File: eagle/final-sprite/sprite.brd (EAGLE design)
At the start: 35 x 44.6 mm, 60 parts, among them J1 M20-7910442R, U1 CC430F513X, U2 LSM9DS1, U4 DRV8837, U5 ADP5092, U6 DRV8837, U7 DRV8837, X1 SPRITEPIN_SPRITE_PIN, X2 SPRITEPIN_SPRITE_PIN

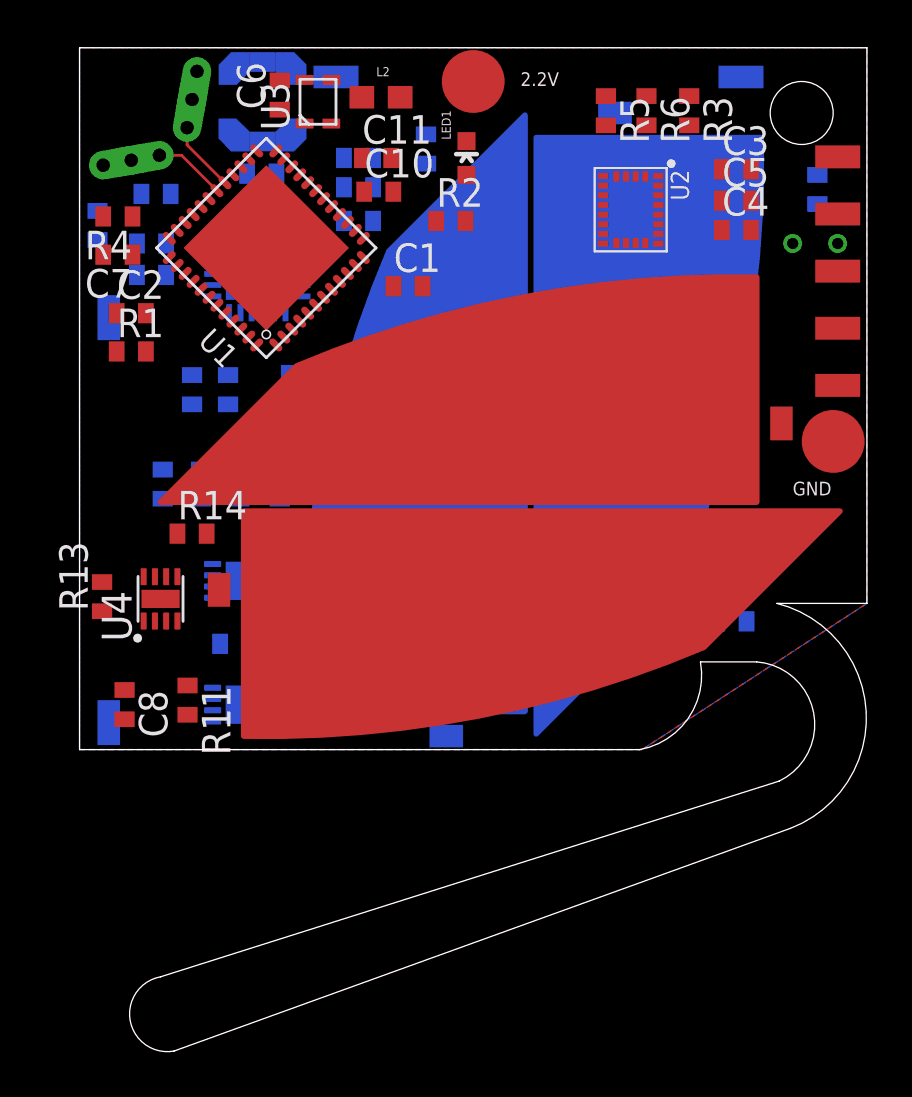
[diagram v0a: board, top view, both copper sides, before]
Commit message: successful autoroute 2 blind capability 69 vias
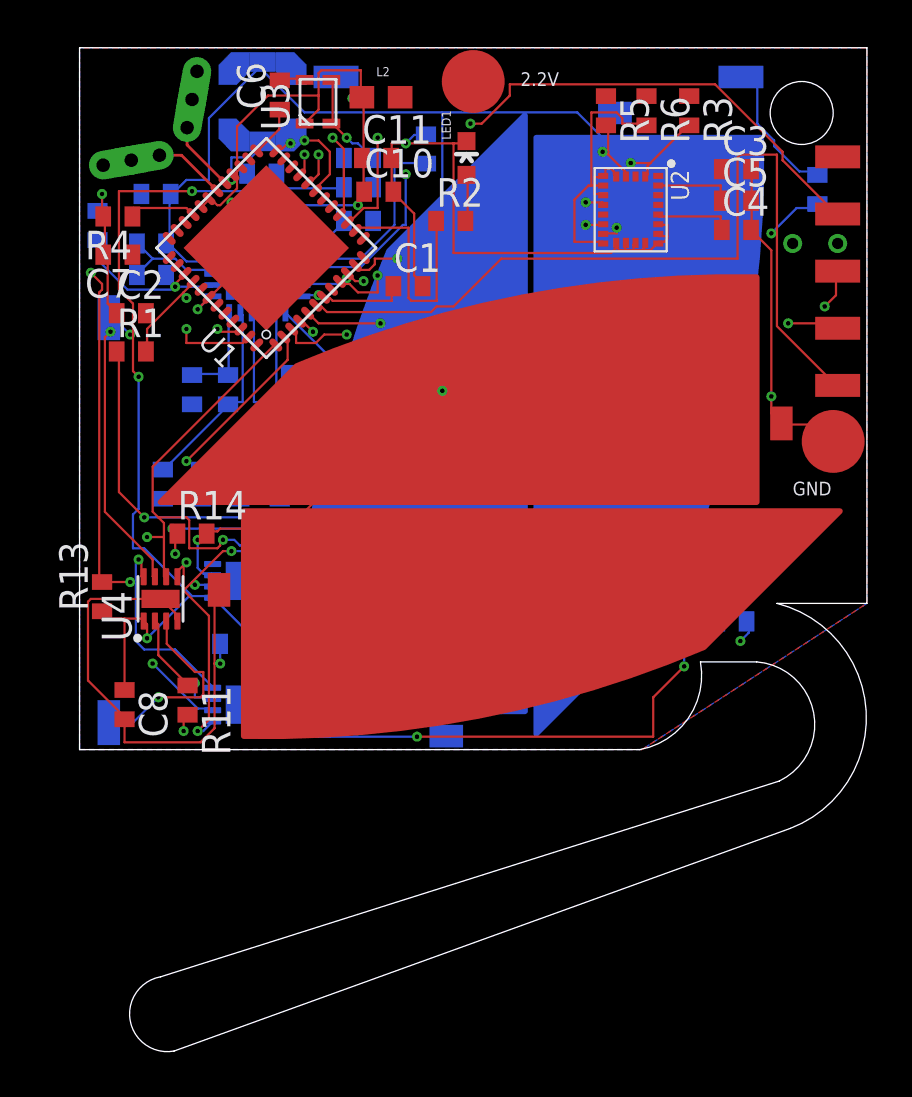
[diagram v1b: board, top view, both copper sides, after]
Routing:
- net VCCINT: track 0.00 -> 88.0 mm, vias 0 -> 1
- net GND: track 0.16 -> 86.0 mm, vias 0 -> 6
- net VCCIO: track 0.00 -> 43.4 mm, vias 0 -> 3
- net RST: track 0.00 -> 40.7 mm, vias 0 -> 2
- net UART_RX: track 0.00 -> 37.6 mm
- net N$26: track 0.00 -> 35.5 mm, vias 0 -> 2
- net VSYS: track 0.00 -> 34.3 mm, vias 0 -> 4
- net TST: track 0.00 -> 34.0 mm, vias 0 -> 2
- net PWM1: track 0.00 -> 32.3 mm, vias 0 -> 3
- net EN_2: track 0.00 -> 31.7 mm, vias 0 -> 2
- net EN_3: track 0.00 -> 28.6 mm, vias 0 -> 2
- net EN_1: track 0.00 -> 28.3 mm, vias 0 -> 2
- net VCC: track 0.00 -> 27.4 mm, vias 0 -> 2
- net VBAT: track 0.00 -> 26.5 mm, vias 0 -> 1
- net N$27: track 0.00 -> 26.5 mm, vias 0 -> 2
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
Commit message: did most of the long traces
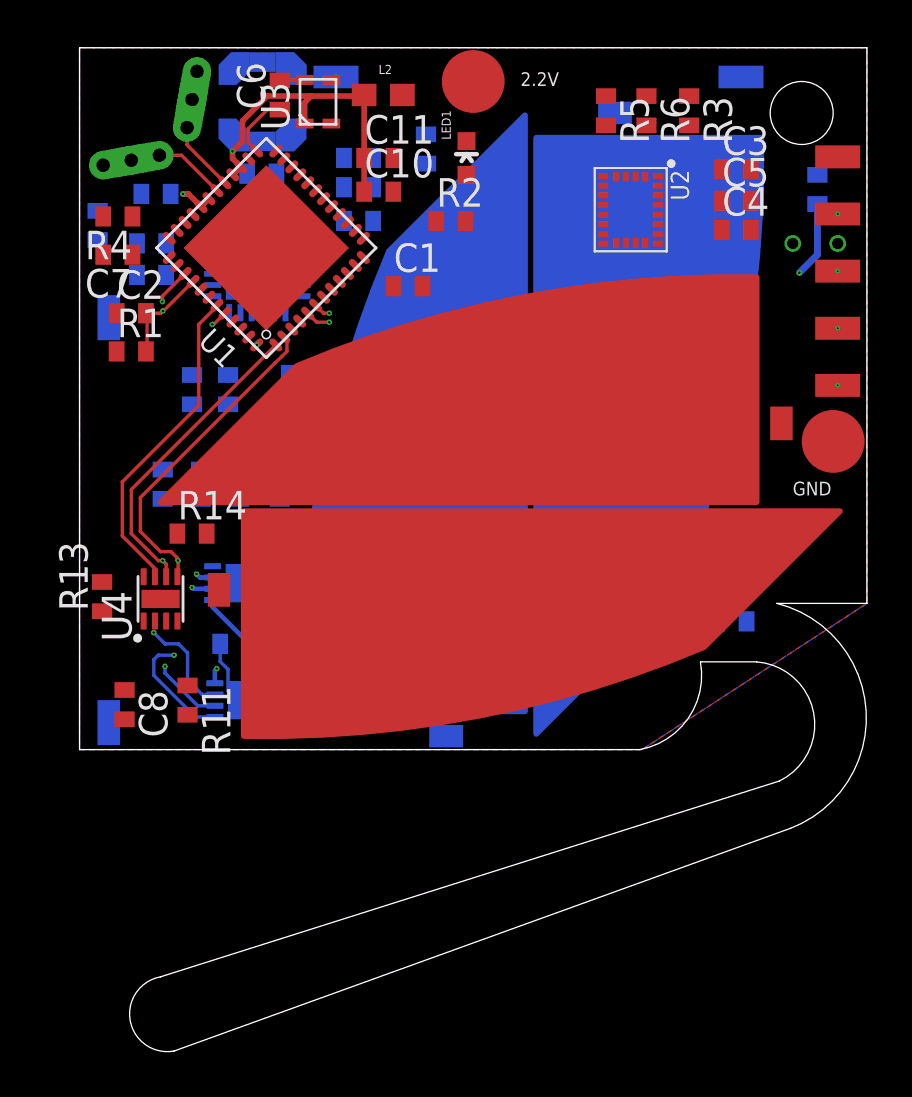
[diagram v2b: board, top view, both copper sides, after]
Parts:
- moved U7 5.40 mm to (6.90, 11.2), turned to 180 degrees
- moved U6 5.30 mm to (7.00, 6.00), turned to 0 degrees
- moved L2 0.14 mm to (13.5, 32.9)
- moved C11 0.10 mm to (13.3, 30.1)
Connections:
- removed net VSYS: C14.1, C15.1, R13.2, R14.1, U5.16
- net EN_1: now also U1.43; no longer U1.19
- net EN_2: now also U1.44; no longer U1.20
- net EN_3: now also U1.48; no longer U1.21
- net VCC: now also C14.1, C15.1, R13.2, R14.1, U5.16
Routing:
- net VCCINT: track 88.0 -> 0.00 mm, vias 1 -> 0
- net GND: track 86.0 -> 4.46 mm, vias 6 -> 0
- net VCCIO: track 43.4 -> 4.56 mm, vias 3 -> 0
- net VSYS: track 34.3 -> 0.00 mm, vias 4 -> 0
- net VCC: track 27.4 -> 4.49 mm
- net UART_TX: track 23.9 -> 45.9 mm
- net N$4: track 21.1 -> 0.00 mm, vias 2 -> 0
- net SCL: track 20.3 -> 0.00 mm, vias 2 -> 0
- net N$28: track 25.1 -> 6.83 mm, vias 2 -> 1
- net INT2: track 17.6 -> 0.00 mm, vias 2 -> 0
- net SDA: track 17.1 -> 0.00 mm, vias 2 -> 0
- net REF: track 16.6 -> 0.00 mm
- net N$13: track 23.7 -> 7.14 mm, vias 2 -> 1
- net INT1: track 16.5 -> 0.00 mm, vias 2 -> 0
- net N$27: track 26.5 -> 42.3 mm
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- added copper zone on layer 2, net GND

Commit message: more stuff done
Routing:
- net VCCINT: track 0.00 -> 31.6 mm, vias 0 -> 2
- added copper zone on layer 1, net VCCINT
- added copper zone on layer 16, net VCCINT

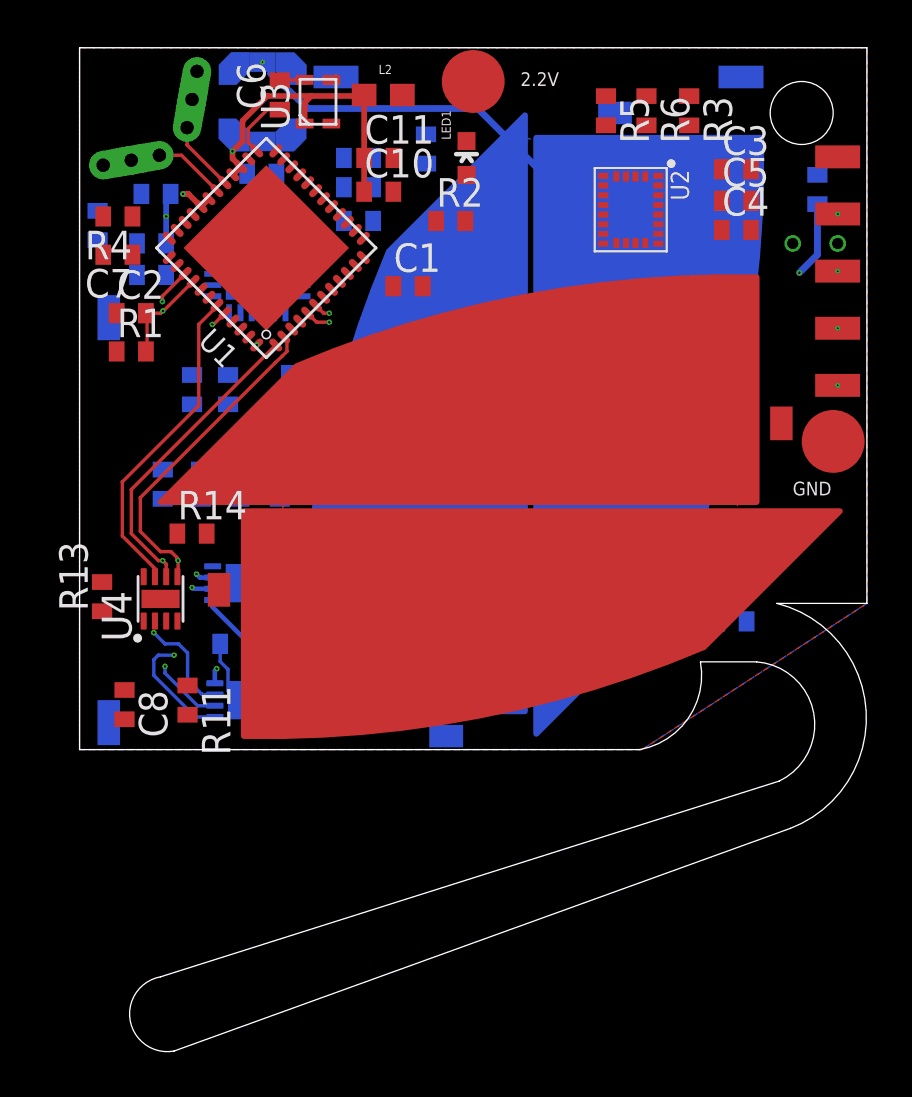
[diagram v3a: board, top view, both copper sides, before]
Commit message: routed some more routes
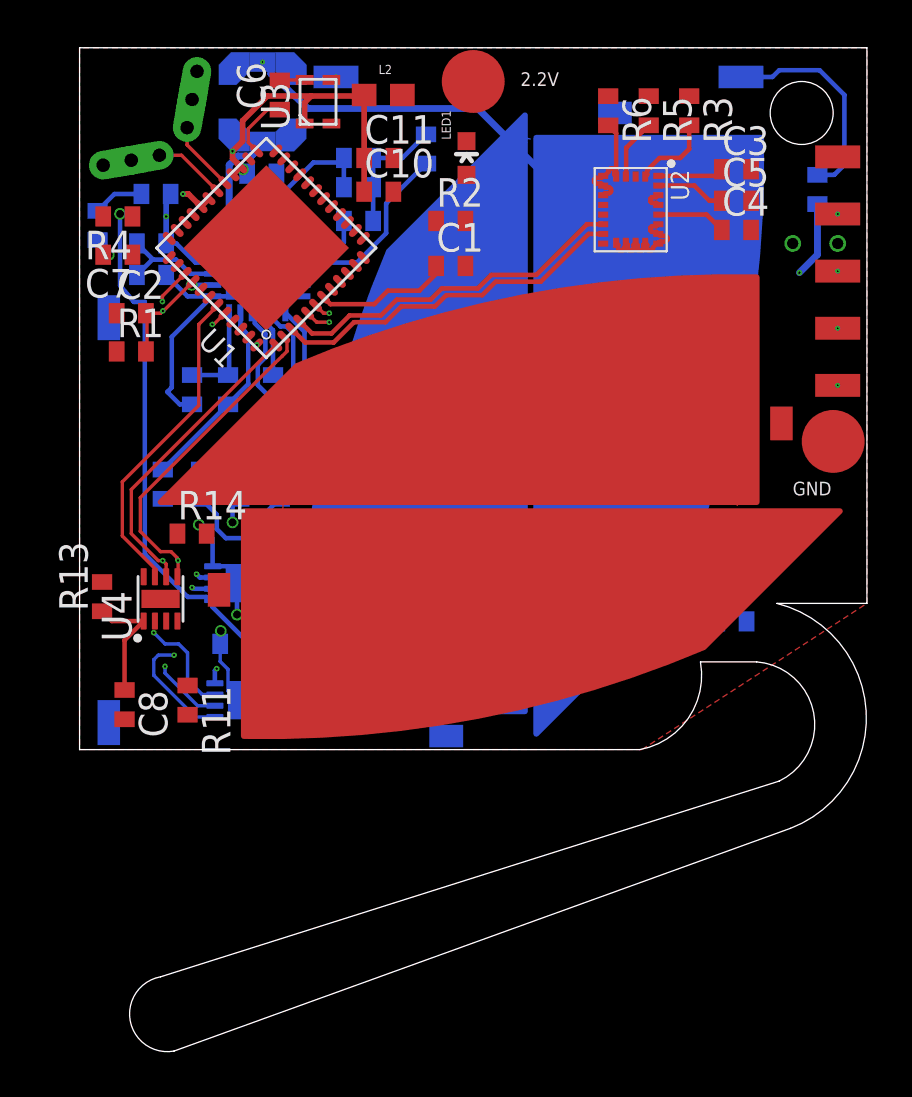
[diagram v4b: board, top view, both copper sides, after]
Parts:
- moved C1 2.10 mm to (16.5, 25.3)
- moved R5 1.90 mm to (25.3, 32.2)
- moved R6 1.70 mm to (23.5, 32.2)
- moved R21 0.81 mm to (8.60, 19.8)
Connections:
- net INT1: now also U1.4; no longer U1.3
- net INT2: now also U1.3; no longer U1.4
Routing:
- net GND: track 4.46 -> 47.1 mm, vias 0 -> 4
- net VCCIO: track 4.56 -> 39.1 mm, vias 0 -> 2
- net REF: track 0.00 -> 16.8 mm
- net INT2: track 0.00 -> 16.1 mm
- net INT1: track 0.00 -> 15.7 mm
- net VCC: track 4.49 -> 14.7 mm
- net TERM: track 0.00 -> 9.99 mm
- net N$9: track 0.00 -> 9.67 mm
- net SETSD: track 0.00 -> 9.52 mm
- net SETPG: track 0.00 -> 8.66 mm
- net N$20: track 0.00 -> 8.12 mm
- net VCORE: track 0.00 -> 6.04 mm
- net N$21: track 0.00 -> 6.04 mm, vias 0 -> 2
- net N$7: track 0.00 -> 5.45 mm
- net N$18: track 0.00 -> 4.93 mm
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- removed copper zone on layer 16, net GND

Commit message: routed all traces, need to do GND and VCC
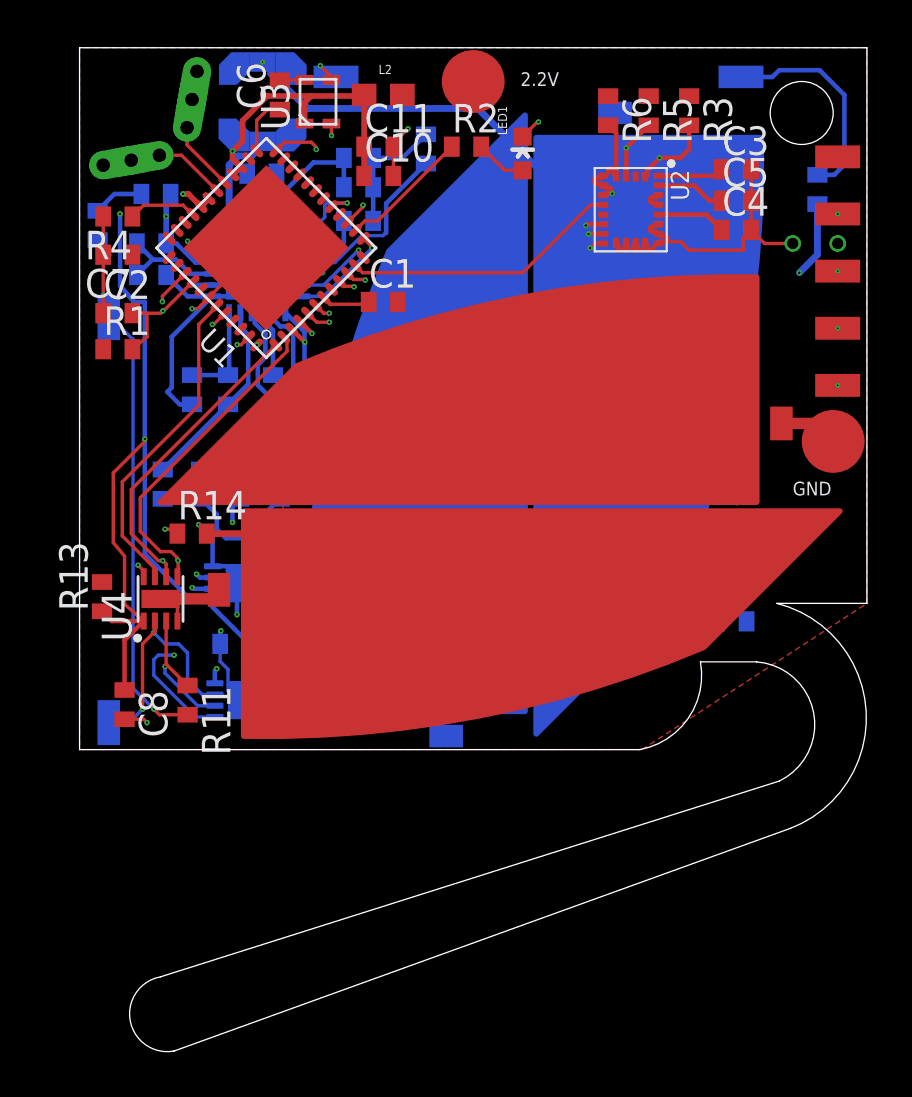
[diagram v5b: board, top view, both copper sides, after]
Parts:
- moved C1 3.40 mm to (13.5, 23.7)
- moved R2 3.37 mm to (17.2, 30.6)
- moved LED1 2.51 mm to (19.7, 30.3)
- moved C10 0.70 mm to (13.3, 29.3)
- moved R1 0.61 mm to (1.70, 21.6)
- moved C2 0.60 mm to (1.70, 23.2)
- moved C11 0.50 mm to (13.3, 30.6)
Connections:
- net N$14: now also U4.2; no longer U4.3
- net N$8: now also U4.3; no longer U4.2
- net PGOOD: now also U1.17; no longer U1.46
- net REG_D1: now also U1.13; no longer U1.16
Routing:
- net GND: track 47.1 -> 77.5 mm, vias 4 -> 11
- net N$4: track 0.00 -> 19.9 mm, vias 0 -> 1
- net SCL: track 3.62 -> 20.4 mm, vias 0 -> 2
- net SDA: track 2.70 -> 17.8 mm, vias 0 -> 2
- net DRDY: track 0.00 -> 12.4 mm
- net DSW: track 0.00 -> 10.2 mm, vias 0 -> 2
- net VCCIO: track 39.1 -> 48.3 mm, vias 2 -> 3
- net REGGOOD: track 0.00 -> 7.48 mm, vias 0 -> 2
- net VCCINT: track 34.0 -> 41.0 mm
- net REG_D0: track 0.00 -> 6.31 mm, vias 0 -> 2
- net N$14: track 0.00 -> 5.89 mm, vias 0 -> 1
- net N$2: track 0.00 -> 5.83 mm
- net REG_D1: track 0.00 -> 4.59 mm, vias 0 -> 1
- net N$7: track 5.45 -> 9.60 mm, vias 0 -> 2
- net VCORE: track 6.04 -> 2.17 mm
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
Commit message: more stuff finished
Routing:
- net VCC: track 18.0 -> 17.6 mm, vias 4 -> 21
- added copper zone on layer 3, net VCC
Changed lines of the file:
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@@
 <grid distance="0.1" unitdist="mm" unit="mm" style="lines" multiple="10" display="yes" altdistance="0.1" altunitdist="mm" altunit="mm"/>
 <layers>
-<layer number="1" name="Top" color="4" fill="1" visible="no" active="yes"/>
-<layer number="2" name="Route2" color="1" fill="3" visible="yes" active="yes"/>
-<layer number="3" name="Route3" color="4" fill="3" visible="no" active="yes"/>
+<layer number="1" name="Top" color="4" fill="1" visible="yes" active="yes"/>
+<layer number="2" name="Route2" color="1" fill="3" visible="no" active="yes"/>
+<layer number="3" name="Route3" color="4" fill="3" visible="yes" active="yes"/>
 <layer number="4" name="Route4" color="1" fill="4" visible="no" active="no"/>
 <layer number="5" name="Route5" color="4" fill="4" visible="no" active="no"/>
@@
 <layer number="14" name="Route14" color="1" fill="6" visible="no" active="no"/>
 <layer number="15" name="Route15" color="4" fill="6" visible="no" active="no"/>
-<layer number="16" name="Bottom" color="1" fill="1" visible="no" active="yes"/>
+<layer number="16" name="Bottom" color="1" fill="1" visible="yes" active="yes"/>
 <layer number="17" name="Pads" color="2" fill="1" visible="yes" active="yes"/>
 <layer number="18" name="Vias" color="2" fill="1" visible="yes" active="yes"/>
@@
 <wire x1="7.9" y1="9.8" x2="7.885" y2="9.815" width="0.2032" layer="16"/>
 <wire x1="7.885" y1="9.815" x2="7.885" y2="10.45" width="0.2032" layer="16"/>
-<wire x1="11.75" y1="28.8" x2="11.75" y2="29.9" width="0.2032" layer="16"/>
-<wire x1="11.75" y1="29.9" x2="11.75" y2="30.1" width="0.2032" layer="16"/>
+<wire x1="11.75" y1="28.8" x2="11.75" y2="30.1" width="0.2032" layer="16"/>
 <wire x1="8.15" y1="27.18" x2="8.2914" y2="27.3214" width="0.2032" layer="16"/>
 <wire x1="8.2914" y1="27.3214" x2="8.2914" y2="27.7943" width="0.2032" layer="16"/>
-<wire x1="8.2914" y1="27.7943" x2="10.3971" y2="29.9" width="0.2032" layer="16"/>
-<wire x1="10.3971" y1="29.9" x2="11.75" y2="29.9" width="0.2032" layer="16"/>
+<wire x1="8.2914" y1="27.7943" x2="9.1971" y2="28.7" width="0.2032" layer="16"/>
 <wire x1="25.725" y1="29.305" x2="28.255" y2="29.305" width="0.2032" layer="1"/>
 <wire x1="28.255" y1="29.305" x2="28.55" y2="29.6" width="0.2032" layer="1"/>
@@
 <wire x1="3.8" y1="13.6" x2="4.15" y2="13.6" width="0.1524" layer="1"/>
 <wire x1="4.15" y1="13.6" x2="4.35" y2="13.4" width="0.1524" layer="1"/>
+<polygon width="0.1524" layer="3">
+<vertex x="11" y="4"/>
+<vertex x="0" y="4"/>
+<vertex x="0" y="29"/>
+<vertex x="6" y="29"/>
+<vertex x="6" y="35"/>
+<vertex x="35" y="35"/>
+<vertex x="35" y="21"/>
+<vertex x="11" y="21"/>
+</polygon>
+<via x="7.4" y="32.9" extent="1-16" drill="0.1016"/>
+<via x="14" y="31.7" extent="1-16" drill="0.1016"/>
+<via x="16.5" y="29.6" extent="1-16" drill="0.1016"/>
+<via x="15.6" y="28.6" extent="1-16" drill="0.1016"/>
+<via x="14.3" y="27.4" extent="1-16" drill="0.1016"/>
+<via x="13.3" y="31.5" extent="1-16" drill="0.1016"/>
+<via x="4.8" y="21.9" extent="1-16" drill="0.1016"/>
+<via x="3.7" y="22.6" extent="1-16" drill="0.1016"/>
+<via x="3.6" y="20.7" extent="1-16" drill="0.1016"/>
+<via x="1.5" y="19.3" extent="1-16" drill="0.1016"/>
+<via x="3.7" y="18.8" extent="1-16" drill="0.1016"/>
+<via x="1.5" y="17.6" extent="1-16" drill="0.1016"/>
+<via x="1.3" y="8.5" extent="1-16" drill="0.1016"/>
+<wire x1="9.1971" y1="28.7" x2="10.2" y2="28.6971" width="0.2032" layer="16"/>
+<wire x1="10.2" y1="28.6971" x2="10.9" y2="28.7" width="0.2032" layer="16"/>
+<via x="10.9" y="28.7" extent="3-16" drill="0.1016"/>
+<wire x1="10.9" y1="28.7" x2="11" y2="28.8" width="0.2032" layer="16"/>
+<wire x1="11" y1="28.8" x2="11.75" y2="28.8" width="0.2032" layer="16"/>
+<via x="3.3" y="14.1" extent="1-16" drill="0.1016"/>
+<via x="5.4" y="9.4" extent="1-16" drill="0.1016"/>
+<via x="5.2" y="7.8" extent="1-16" drill="0.1016"/>
 <wire x1="25.725" y1="29.305" x2="24.715" y2="29.275" width="0" layer="19" extent="1-1"/>
 <wire x1="25.725" y1="28.445" x2="25.725" y2="29.305" width="0" layer="19" extent="1-1"/>
-<wire x1="10.3971" y1="29.9" x2="9.43136875" y2="29.70624375" width="0" layer="19" extent="1-16"/>
 <wire x1="6.815075" y1="22.84730625" x2="5.400859375" y2="24.261521875" width="0" layer="19" extent="1-1"/>
 <wire x1="4.693753125" y1="27.23136875" x2="2.35" y2="25.8" width="0" layer="19" extent="1-1"/>
 <wire x1="11.1991375" y1="24.261521875" x2="8.15" y2="27.18" width="0" layer="19" extent="1-16"/>
-<wire x1="7.885" y1="10.45" x2="4.35" y2="13.4" width="0" layer="19" extent="1-16"/>
 </signal>
 <signal name="GND">
@@
 <wire x1="33.55" y1="29.35" x2="32.8" y2="29.35" width="0.2032" layer="16"/>
 </signal>
+<signal name="N$17">
+<via x="16.3" y="31.6" extent="1-16" drill="0.1016"/>
+</signal>
 </signals>
